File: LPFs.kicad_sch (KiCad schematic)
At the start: 21 parts

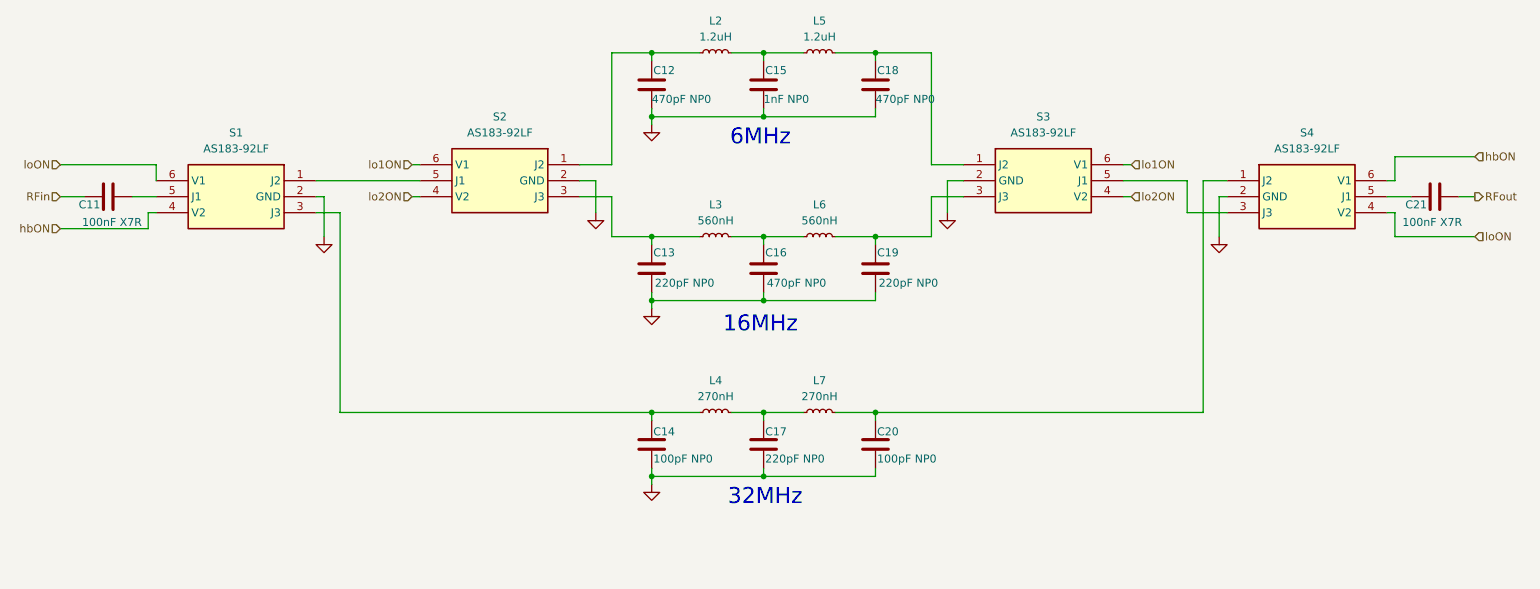
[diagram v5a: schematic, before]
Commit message: Fixes to pass ERC. Nothing serious really.
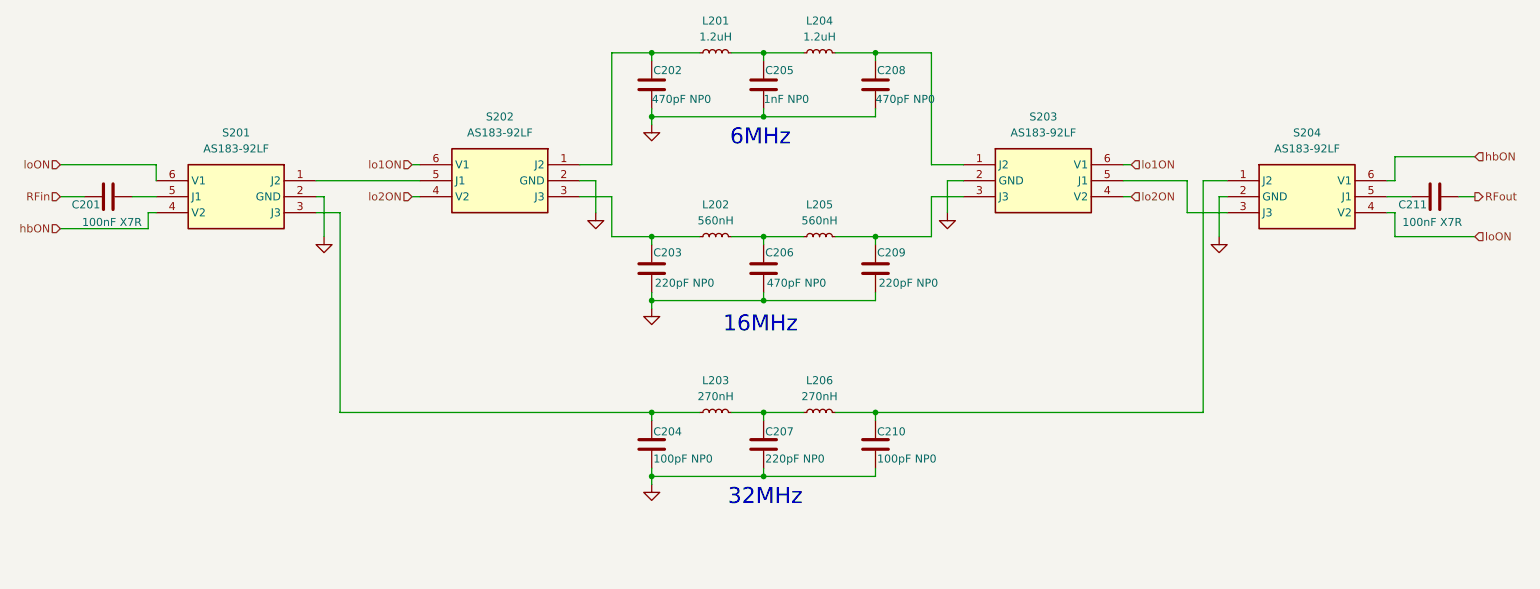
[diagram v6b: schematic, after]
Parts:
- S201: renamed from S1; footprint SOT65P220X110-6N -> Library:SOT65P220X110-6N; Manufacturer_Part_Number (none) -> AS183-92LF
- S202: renamed from S2; footprint SOT65P220X110-6N -> Library:SOT65P220X110-6N; Manufacturer_Part_Number (none) -> AS183-92LF
- S203: renamed from S3; footprint SOT65P220X110-6N -> Library:SOT65P220X110-6N; Manufacturer_Part_Number (none) -> AS183-92LF
- S204: renamed from S4; footprint SOT65P220X110-6N -> Library:SOT65P220X110-6N; Manufacturer_Part_Number (none) -> AS183-92LF
- renumbered C11 to C201, C12 to C202, C13 to C203, C14 to C204, C15 to C205, C16 to C206, C17 to C207, C18 to C208, C19 to C209, C20 to C210, C21 to C211, L2 to L201, L3 to L202, L4 to L203, L5 to L204, L6 to L205, L7 to L206

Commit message: Tarted up, 3d models applied, better footprints and BOM, ready to submit for PCBA
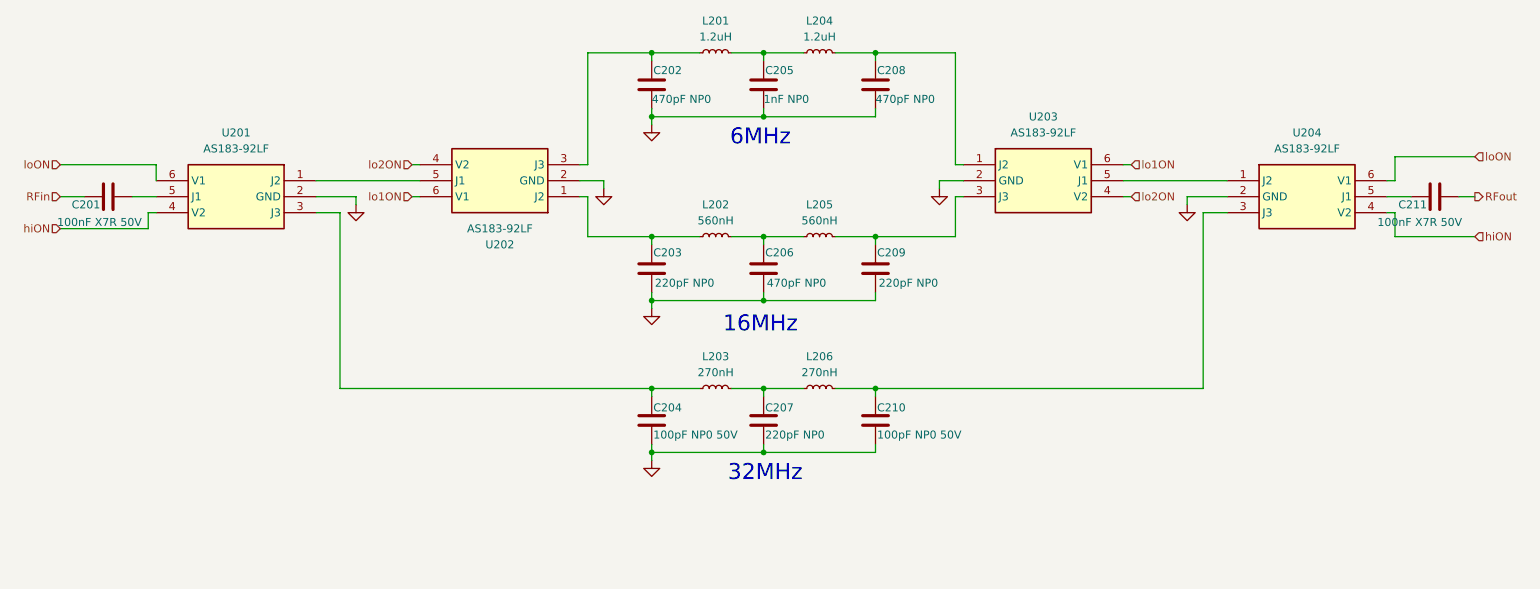
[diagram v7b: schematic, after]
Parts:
- C201, C211: value 100nF X7R -> 100nF X7R 50V; LCSC C14663 -> C24452
- C202, C206, C208: footprint Capacitor_SMD:C_0603_1608Metric -> Capacitor_SMD:C_0402_1005Metric; LCSC C106211 -> C106259
- C203, C207, C209: footprint Capacitor_SMD:C_0603_1608Metric -> Capacitor_SMD:C_0402_1005Metric; LCSC C106210 -> C107001
- C204, C210: value 100pF NP0 -> 100pF NP0 50V; footprint Capacitor_SMD:C_0603_1608Metric -> Capacitor_SMD:C_0402_1005Metric; LCSC C14665 -> C106200
- C205: footprint Capacitor_SMD:C_0603_1608Metric -> Capacitor_SMD:C_0402_1005Metric; LCSC C1588 -> C5182455
- L201, L204: LCSC C46470448 -> C703714
- L202, L205: LCSC C20417044 -> C6364717
- L203, L206: LCSC C20623520 -> C404430
- renumbered S201 to U201, S202 to U202, S203 to U203, S204 to U204
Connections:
- net loON: now also U204.6 (V1); no longer U204.4 (V2)
- net at C210.1, L206.2: now also U204.3 (J3); no longer U204.1 (J2)
- net at U203.5 (J1): now also U204.1 (J2); no longer U204.3 (J3)
- net at C202.1, L201.1: now also U202.3 (J3); no longer U202.1 (J2)
- net at C203.1, L202.1: now also U202.1 (J2); no longer U202.3 (J3)
- net hbON renamed hiON
- net hiON: now also U204.4 (V2); no longer U204.6 (V1)
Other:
- moved on the sheet: C204, C207, C210, L203, L206, U202

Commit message: Small changes to part numbers to ease supply chain issues for build
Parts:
- L201, L204: LCSC C703714 -> C2044063
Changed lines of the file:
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@@
 			)
 		)
-		(property "LCSC" "C703714"
+		(property "LCSC" "C2044063"
 			(at 132.08 34.29 90)
 			(effects
@@
 			)
 		)
-		(property "LCSC" "C703714"
+		(property "LCSC" "C2044063"
 			(at 148.59 34.29 90)
 			(effects
